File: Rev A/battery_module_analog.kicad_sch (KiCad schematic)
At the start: 0 parts

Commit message: Analog MPPT
Current sensing and voltage sensing circuits that go into the TL494 to change the PWM signal that will go into the buck converter. This schematic shows how to change the oscillation frequency of the TL494 and also provides a Voltage Protection to shut down all outputs of the TL494 in case of voltage spike.
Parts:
- added C1: 100nF, symbol Device:C
- added C5: 1nF, symbol Device:C
- added D5: LED, symbol Device:LED
- added D6: 1N4148, Diode_THT:D_DO-35_SOD27_P7.62mm_Horizontal, symbol Diode:1N4148
- added F2: 10A, symbol Device:Fuse
- added Q3: BC557, Package_TO_SOT_THT:TO-92_Inline, symbol Transistor_BJT:BC557
- added R1, R18, R19, R22, R25, R7, R9: 10K, symbol Device:R
- added R10, R15, R16: 47K, symbol Device:R
- added R11: 56k, symbol Device:R
- added R12: 0R1, symbol Device:R
- added R13, R14, R23: 2K, symbol Device:R
- added R17: 560R, symbol Device:R
- added R2: 6K8, symbol Device:R
- added R20: 39K, symbol Device:R
- added R21, R24: 2K2, symbol Device:R
- added R8: 1K, symbol Device:R
- added RV1, RV2: 10K, symbol Device:R_Potentiometer
- added U1: TL494, symbol Regulator_Controller:TL494
- added U2: LM358, symbol Amplifier_Operational:LM358
- added U3: TL431D, Package_SO:SOIC-8_3.9x4.9mm_P1.27mm, symbol Reference_Voltage:TL431D
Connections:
- new net: R18.2, R19.1, U1.15 (2IN-)
- new net: C1.1, R10.2
- new net: C1.2, R11.2, U1.3 (FB)
- new net: R7.2, R8.2, R9.1
- new net: F2.1, R1.1
- new net: R1.2, RV1.1, RV1.2
- new net: R10.1, R11.1, R8.1, U1.2 (1IN-)
- new net: R2.1, RV1.3, U1.1 (1IN+)
- new net: R12.1, R13.2
- new net: R14.2, R15.1, U2.3 (+)
- new net: R20.1, U1.6 (RT)
- new net: R17.1, RV2.3, U1.16 (2IN+)
- new net: C5.1, U1.5 (CT)
- new net: R16.1, RV2.1, RV2.2, U2.1
- new net: R13.1, R16.2, U2.2 (-)
- new net: D5.1 (K), D6.1 (K), U3.1 (K)
- new net: D6.2 (A), Q3.2 (B), R25.2
- new net: D5.2 (A), R21.2
- new net: R22.2, R23.1, U3.8 (REF)
- new net 5V Out: U1.14 (REF)
- new net Battery (+Terminal): F2.2, R21.1, R22.1
- new net Battery (-Terminal): R12.2, R14.1
- new net GND: C5.2, R15.2, R17.2, R19.2, R2.2, R20.2, R23.2, R24.2, R9.2, U1.10 (E2), U1.13 (OUTCTRL), U1.7 (GND), U1.9 (E1), U3.2 (A), U3.3 (A), U3.6 (A), U3.7 (A)
- new net PMW Output to Buck Converter: U1.11 (C2), U1.8 (C1)
- new net Pin 14: Q3.3 (E), R18.1, R25.1, R7.1
- new net To Solar Input: U1.12 (VCC)
- new net VC Out: Q3.1 (C), R24.1
- new net VP Out: U1.4 (DTC)

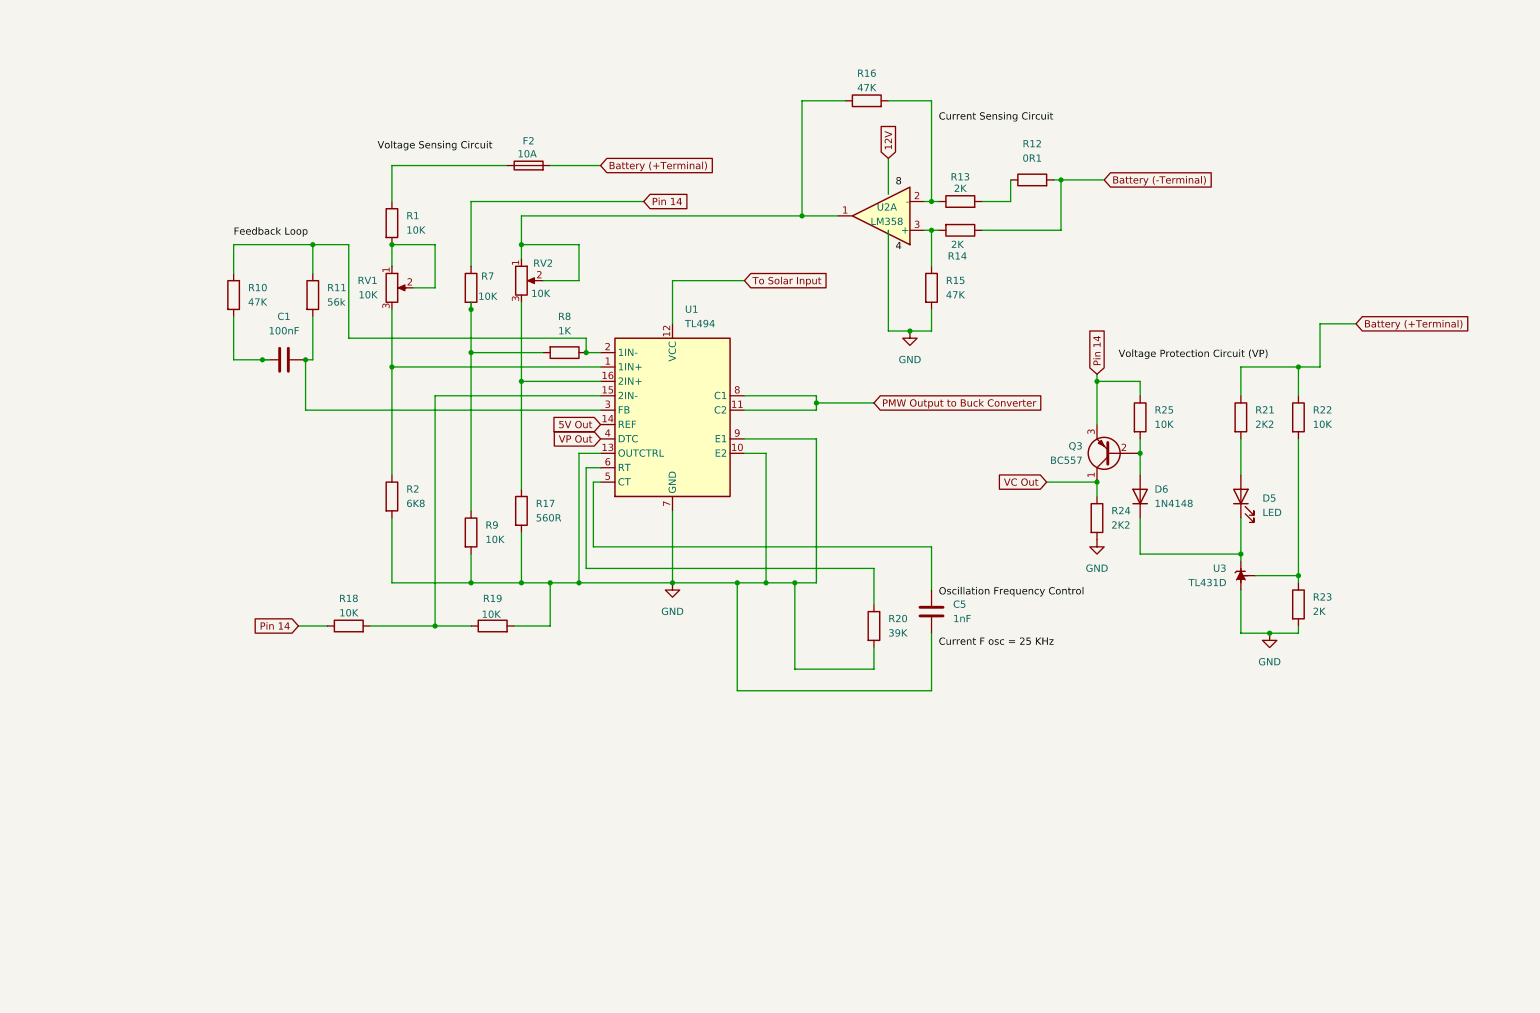
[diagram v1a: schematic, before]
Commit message: Analog MPPT (Latest Update)
Cleaned connections.
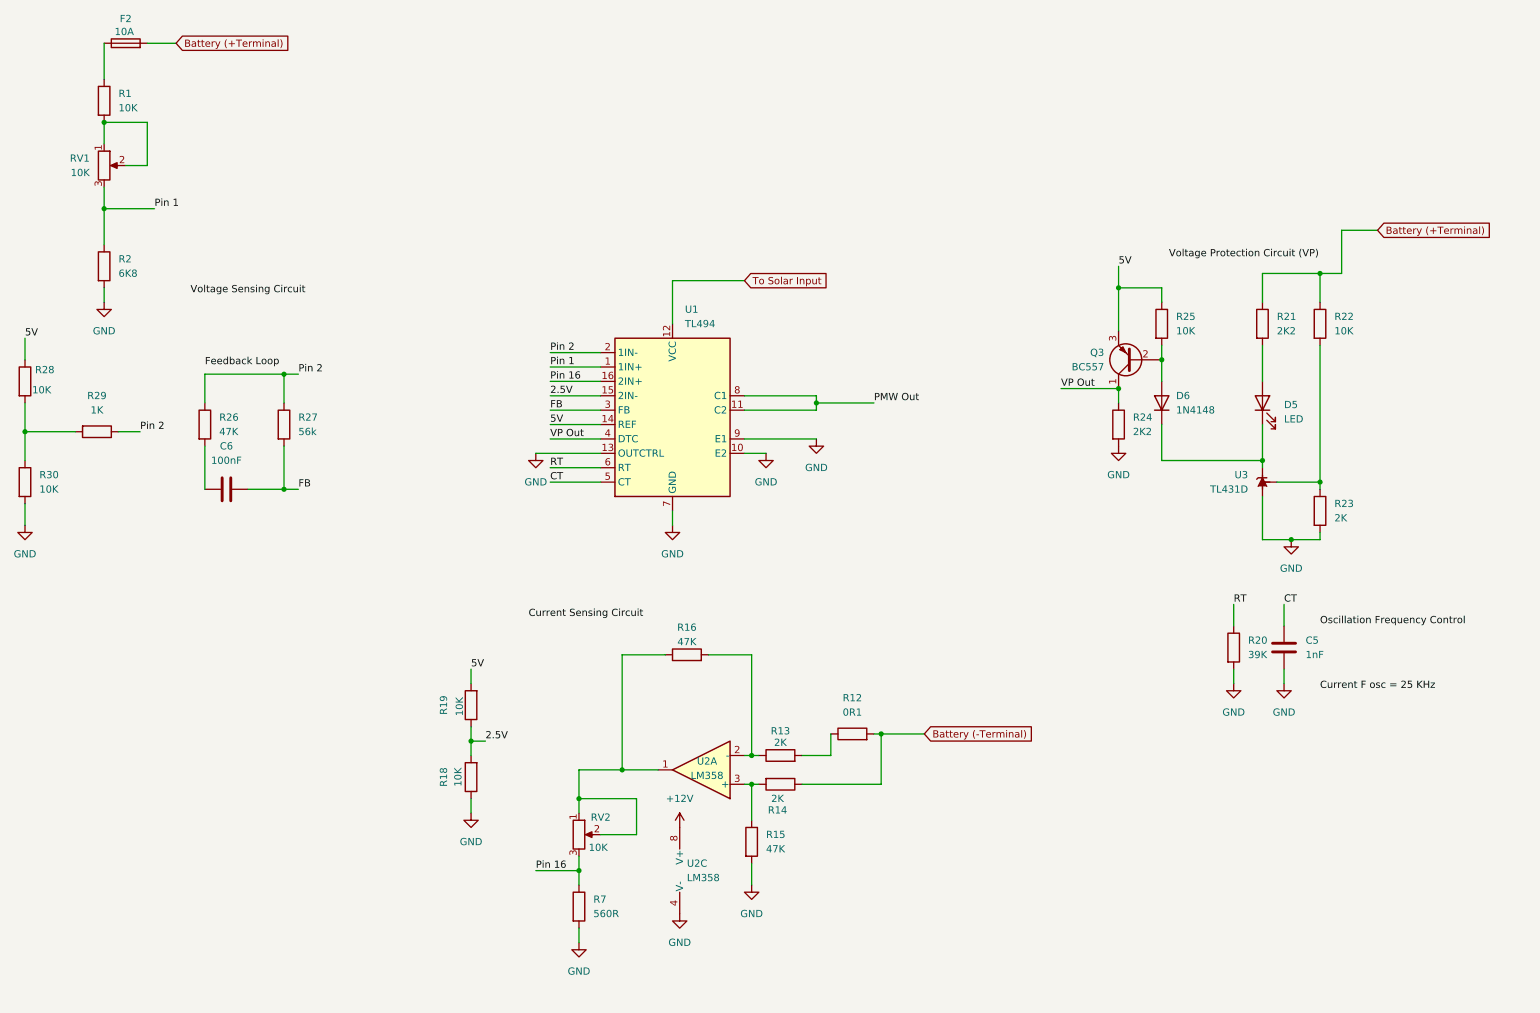
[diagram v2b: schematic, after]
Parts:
- removed C1: 100nF, symbol Device:C
- removed R10: 47K, symbol Device:R
- removed R11: 56k, symbol Device:R
- removed R17: 560R, symbol Device:R
- removed R8: 1K, symbol Device:R
- removed R9: 10K, symbol Device:R
- added C6: 100nF, symbol Device:C
- added R26: 47K, symbol Device:R
- added R27: 56k, symbol Device:R
- added R28, R30: 10K, symbol Device:R
- added R29: 1K, symbol Device:R
- added unit 3 of U2
- R7: value 10K -> 560R
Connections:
- net VC Out is gone; now on net VP Out: Q3.1 (C), R24.1
- net GND: now also R18.1, R7.2, R30.2, U2.4 (V-); no longer R19.2
- net 2.5V: now reaches R18.2, R19.1, U1.15 (2IN-)
- net FB: now reaches U1.3 (FB)
- net FB: now also C6.2, R27.2
- net Pin 2: now reaches U1.2 (1IN-)
- net Pin 2: now also R26.1, R27.1, R29.1
- net Pin 1: now reaches R2.1, RV1.3, U1.1 (1IN+)
- net RT: now reaches R20.1, U1.6 (RT)
- net Pin 16: now reaches RV2.3, U1.16 (2IN+)
- net Pin 16: now also R7.1
- net CT: now reaches C5.1, U1.5 (CT)
- net 5V Out renamed 5V
- net 5V: now also Q3.3 (E), R19.2, R25.1, R28.1
- net PMW Output to Buck Converter renamed PMW Out
- removed net Pin 14: Q3.3 (E), R18.1, R25.1, R7.1
- new net: C6.1, R26.2
- new net: R28.2, R29.2, R30.1
- new net +12V: U2.8 (V+)
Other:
- moved on the sheet: C5, D5, D6, Q3, R1, R12, R13, R14, R15, R16, R18, R19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

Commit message: Updated MPPT
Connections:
- net Pin 1 renamed Pin1
- net Pin 16 renamed Pin16
- net Pin 2 renamed Pin2
- net VP Out renamed VPOut
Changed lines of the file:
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@@
 		)
 	)
-	(label "VP Out"
+	(label "VPOut"
 		(at 115.57 95.25 0)
 		(fields_autoplaced yes)
@@
 		)
 	)
-	(label "Pin 16"
+	(label "Pin16"
 		(at 113.03 171.45 0)
 		(fields_autoplaced yes)
@@
 		)
 	)
-	(label "Pin 2"
+	(label "Pin2"
 		(at 71.12 83.82 0)
 		(fields_autoplaced yes)
@@
 		)
 	)
-	(label "Pin 2"
+	(label "Pin2"
 		(at 43.18 93.98 0)
 		(fields_autoplaced yes)
@@
 		)
 	)
-	(label "Pin 1"
+	(label "Pin1"
 		(at 45.72 54.61 0)
 		(fields_autoplaced yes)
@@
 		)
 	)
-	(label "Pin 1"
+	(label "Pin1"
 		(at 115.57 82.55 0)
 		(fields_autoplaced yes)
@@
 		)
 	)
-	(label "Pin 16"
+	(label "Pin16"
 		(at 115.57 85.09 0)
 		(fields_autoplaced yes)
@@
 		)
 	)
-	(label "VP Out"
+	(label "VPOut"
 		(at 205.74 86.36 0)
 		(fields_autoplaced yes)
@@
 		)
 	)
-	(label "Pin 2"
+	(label "Pin2"
 		(at 115.57 80.01 0)
 		(fields_autoplaced yes)

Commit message: mppt schematic (03/30/2024)
Used 5V to power up op amp. Changed configurations of potentiometers.
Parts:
- removed RV1: 10K, symbol Device:R_Potentiometer
- R2: value 6K8 -> 2.2K
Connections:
- net Pin1 is gone; now on net EA1+: R2.1, U1.1 (1IN+)
- net EA1+: now reaches R1.2
- net at R16.1, RV2.1, U2.1: no longer RV2.2
- net +12V renamed +5V
- net 2.5V renamed EA2-
- net 5V renamed VREF
- net Battery (+Terminal) renamed BAT+
- net Battery (-Terminal) renamed BAT-
- net PMW Out renamed PWM Out
- net Pin16 renamed EA2+
- net EA2+: now also RV2.2; no longer RV2.3
- net Pin2 renamed EA1-
- net To Solar Input renamed SOLAR+
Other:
- note added: "Add buck converter to go from solar to 12 V (LDO)"
- note added: "Change potentiometer to voltage divider to get around 2.5 V. Assumed Vin = 14V"
- note added: "Current Sensing Circuit"
- note added: "Feedback Loop"
- note added: "Fosc = 25 KHz"
- note added: "Note: Change Label Names"
- note added: "Note: Connect RV2 (2) to resistor and don't connect (3) to anything"
- note added: "Oscillation Frequency Control"
- note added: "Voltage Protection Circuit (VP)"
- note added: "Voltage Sensing Circuit"

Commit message: Updated PCB and Schematics
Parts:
- C5, C6: footprint (none) -> Capacitor_SMD:C_0805_2012Metric_Pad1.18x1.45mm_HandSolder
- D5: footprint (none) -> Diode_SMD:D_3220_8050Metric_Pad2.65x5.15mm_HandSolder
- F2: footprint (none) -> Fuse:Fuse_0805_2012Metric_Pad1.15x1.40mm_HandSolder
- R1, R12, R13, R14, R15, R16, R18, R19, R2, R20, R21, R22, R23, R24, R25, R26, R27, R28, R29, R30, R7: footprint (none) -> Resistor_SMD:R_0805_2012Metric_Pad1.20x1.40mm_HandSolder
- RV2: footprint (none) -> Potentiometer_THT:Potentiometer_Bourns_3339P_Vertical_HandSoldering
- U1: footprint (none) -> Package_DIP:DIP-16_W7.62mm_Socket
- U2: footprint (none) -> Package_DIP:DIP-8_W7.62mm_Socket
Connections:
- net +5V is gone; now on net VREF: U2.8 (V+)
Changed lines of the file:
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@@
 	)
 	(label "VREF"
+		(at 138.43 163.83 0)
+		(fields_autoplaced yes)
+		(effects
+			(font
+				(size 1.27 1.27)
+			)
+			(justify left bottom)
+		)
+	)
+	(label "VREF"
 		(at 115.57 92.71 0)
 		(fields_autoplaced yes)
@@
 			)
 		)
-		(property "Footprint" ""
+		(property "Footprint" "Resistor_SMD:R_0805_2012Metric_Pad1.20x1.40mm_HandSolder"
 			(at 103.378 142.24 90)
 			(effects
@@
 			)
 		)
-		(property "Footprint" ""
+		(property "Footprint" "Resistor_SMD:R_0805_2012Metric_Pad1.20x1.40mm_HandSolder"
 			(at 66.802 92.71 90)
 			(effects
@@
 			)
 		)
-		(property "Footprint" ""
+		(property "Footprint" "Resistor_SMD:R_0805_2012Metric_Pad1.20x1.40mm_HandSolder"
 			(at 35.052 35.56 90)
 			(effects
@@
 			)
 		)
-		(property "Footprint" ""
+		(property "Footprint" "Capacitor_SMD:C_0805_2012Metric_Pad1.18x1.45mm_HandSolder"
 			(at 62.23 103.1748 0)
 			(effects
@@
 			)
 		)
-		(property "Footprint" ""
+		(property "Footprint" "Resistor_SMD:R_0805_2012Metric_Pad1.20x1.40mm_HandSolder"
 			(at 52.832 92.71 90)
 			(effects
@@
 			)
 		)
-		(property "Footprint" ""
+		(property "Footprint" "Resistor_SMD:R_0805_2012Metric_Pad1.20x1.40mm_HandSolder"
 			(at 168.91 149.098 90)
 			(effects
@@
 			)
 		)
-		(property "Footprint" ""
+		(property "Footprint" "Resistor_SMD:R_0805_2012Metric_Pad1.20x1.40mm_HandSolder"
 			(at 156.21 154.432 90)
 			(effects
@@
 			)
 		)
-		(property "Footprint" ""
+		(property "Footprint" "Resistor_SMD:R_0805_2012Metric_Pad1.20x1.40mm_HandSolder"
 			(at 118.872 177.8 90)
 			(effects
@@
 			)
 		)
-		(property "Footprint" ""
+		(property "Footprint" "Resistor_SMD:R_0805_2012Metric_Pad1.20x1.40mm_HandSolder"
 			(at 149.352 166.37 90)
 			(effects
@@
 			)
 		)
-		(property "Footprint" ""
+		(property "Footprint" "Resistor_SMD:R_0805_2012Metric_Pad1.20x1.40mm_HandSolder"
 			(at 21.082 85.09 90)
 			(effects
@@
 			)
 		)
-		(property "Footprint" ""
+		(property "Footprint" "Resistor_SMD:R_0805_2012Metric_Pad1.20x1.40mm_HandSolder"
 			(at 234.442 132.08 90)
 			(effects
@@
 			)
 		)
-		(property "Footprint" ""
+		(property "Footprint" "Fuse:Fuse_0805_2012Metric_Pad1.15x1.40mm_HandSolder"
 			(at 40.64 27.178 90)
 			(effects
@@
 			)
 		)
-		(property "Footprint" ""
+		(property "Footprint" "Capacitor_SMD:C_0805_2012Metric_Pad1.18x1.45mm_HandSolder"
 			(at 246.0752 135.89 0)
 			(effects
@@
 			)
 		)
-		(property "Footprint" ""
+		(property "Footprint" "Resistor_SMD:R_0805_2012Metric_Pad1.20x1.40mm_HandSolder"
 			(at 139.7 135.128 90)
 			(effects
@@
 			)
 		)
-		(property "Footprint" ""
+		(property "Footprint" "Resistor_SMD:R_0805_2012Metric_Pad1.20x1.40mm_HandSolder"
 			(at 21.082 102.87 90)
 			(effects
@@
 			)
 		)
-		(property "Footprint" ""
+		(property "Footprint" "Diode_SMD:D_3220_8050Metric_Pad2.65x5.15mm_HandSolder"
 			(at 241.3 88.9 0)
 			(effects
@@
 			)
 		)
-		(property "Footprint" ""
+		(property "Footprint" "Resistor_SMD:R_0805_2012Metric_Pad1.20x1.40mm_HandSolder"
 			(at 35.052 48.26 90)
 			(effects
@@
 			)
 		)
-		(property "Footprint" ""
+		(property "Footprint" "Resistor_SMD:R_0805_2012Metric_Pad1.20x1.40mm_HandSolder"
 			(at 214.122 92.71 90)
 			(effects
@@
 			)
 		)
-		(property "Footprint" ""
+		(property "Footprint" "Resistor_SMD:R_0805_2012Metric_Pad1.20x1.40mm_HandSolder"
 			(at 249.682 74.93 90)
 			(effects
@@
 			)
 		)
-		(property "Footprint" ""
+		(property "Footprint" "Resistor_SMD:R_0805_2012Metric_Pad1.20x1.40mm_HandSolder"
 			(at 249.682 107.95 90)
 			(effects
@@
 			)
 		)
-		(property "Footprint" ""
+		(property "Footprint" "Resistor_SMD:R_0805_2012Metric_Pad1.20x1.40mm_HandSolder"
 			(at 156.21 152.908 90)
 			(effects
@@
 			)
 		)
-		(property "Footprint" ""
+		(property "Footprint" "Potentiometer_THT:Potentiometer_Bourns_3339P_Vertical_HandSoldering"
 			(at 120.65 165.1 0)
 			(effects
@@
 			)
 		)
-		(property "Footprint" ""
+		(property "Footprint" "Package_DIP:DIP-16_W7.62mm_Socket"
 			(at 137.16 92.71 0)
 			(effects
@@
 			)
 		)
-		(property "Footprint" ""
+		(property "Footprint" "Resistor_SMD:R_0805_2012Metric_Pad1.20x1.40mm_HandSolder"
 			(at 103.378 154.94 90)
 			(effects
@@
 			)
 		)
-		(property "Footprint" ""
+		(property "Footprint" "Resistor_SMD:R_0805_2012Metric_Pad1.20x1.40mm_HandSolder"
 			(at 239.522 74.93 90)
 			(effects
@@
 			)
 		)
-		(property "Footprint" ""
+		(property "Footprint" "Resistor_SMD:R_0805_2012Metric_Pad1.20x1.40mm_HandSolder"
 			(at 221.742 74.93 90)
 			(effects
@@
 			)
 		)
-		(property "Footprint" ""
+		(property "Footprint" "Package_DIP:DIP-8_W7.62mm_Socket"
 			(at 142.24 153.67 0)
 			(effects
@@
 	)
 	(symbol
-		(lib_id "power:+12V")
-		(at 138.43 163.83 0)
-		(unit 1)
-		(exclude_from_sim no)
-		(in_bom yes)
-		(on_board yes)
-		(dnp no)
-		(property "Reference" "#PWR020"
-			(at 138.43 167.64 0)
-			(effects
-				(font
-					(size 1.27 1.27)
-				)
-				(hide yes)
-			)
-		)
-		(property "Value" "+5V"
-			(at 136.398 160.02 0)
-			(effects
-				(font
-					(size 1.27 1.27)
-				)
-				(justify left)
-			)
-		)
-		(property "Footprint" ""
-			(at 138.43 163.83 0)
-			(effects
-				(font
-					(size 1.27 1.27)
-				)
-				(hide yes)
-			)
-		)
-		(property "Datasheet" ""
-			(at 138.43 163.83 0)
-			(effects
-				(font
-					(size 1.27 1.27)
-				)
-				(hide yes)
-			)
-		)
-		(property "Description" "Power symbol creates a global label with name \"+12V\""
-			(at 138.43 163.83 0)
-			(effects
-				(font
-					(size 1.27 1.27)
-				)
-				(hide yes)
-			)
-		)
-		(pin "1"
-		)
-		(instances
-			(project "SurgicalLightBatteryModule"
-				(path "/352d7abe-fc72-4473-8b68-62eecf44f496/9e5105b1-8c1f-4649-b5a7-96458368c4ee"
-					(reference "#PWR020")
-					(unit 1)
-				)
-			)
-		)
-	)
-	(symbol
 		(lib_id "Device:R")
 		(at 35.56 93.98 270)
@@
 			)
 		)
-		(property "Footprint" ""
+		(property "Footprint" "Resistor_SMD:R_0805_2012Metric_Pad1.20x1.40mm_HandSolder"
 			(at 35.56 92.202 90)
 			(effects
@@
 			)
 		)
-		(property "Footprint" ""
+		(property "Footprint" "Package_DIP:DIP-8_W7.62mm_Socket"
 			(at 140.97 171.45 0)
 			(effects
